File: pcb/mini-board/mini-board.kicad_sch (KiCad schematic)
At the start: 22 parts, among them J1 USB_B, J2 EXPBUS1, J4 Atmel-JTAG-10, SW1 RESET, SW2 NMI, SW3 SW_SPDT, U1 74AC14, U2 W65C02, U3 ATF1502AS-PLCC44, X1 14 MHz

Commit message: Expanding README.md
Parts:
- removed C5: 100nF, Capacitor_THT:C_Disc_D5.0mm_W2.5mm_P5.00mm, symbol Device:C
- removed J2: EXPBUS1, Connector_PinHeader_2.54mm:PinHeader_2x20_P2.54mm_Vertical, symbol Connector_Generic:Conn_02x20_Odd_Even
- removed R1, R4: 1k, Resistor_THT:R_Axial_DIN0207_L6.3mm_D2.5mm_P7.62mm_Horizontal, symbol Device:R
- removed SW1: RESET, Button_Switch_THT:SW_PUSH_6mm, symbol Switch:SW_Push
- removed U1: 74AC14, Package_DIP:DIP-14_W7.62mm_Socket, symbol 74xx:74HC14
- removed U3: ATF1502AS-PLCC44, Package_LCC:PLCC-44_THT-Socket, symbol atf1504as-plcc44:ATF1504AS-xJx44
- added C33, C34, C35, C36: 100nF, Capacitor_THT:C_Disc_D5.0mm_W2.5mm_P5.00mm, symbol Device:C
- added H1, H2, H3, H4: MountingHole, MountingHole:MountingHole_3.2mm_M3_DIN965_Pad_TopOnly, symbol Mechanical:MountingHole
- added J5: Conn_02x18_Odd_Even, Connector_PinHeader_2.54mm:PinHeader_2x18_P2.54mm_Vertical, symbol Connector_Generic:Conn_02x18_Odd_Even
- added R7, R9: 10k, Resistor_THT:R_Axial_DIN0207_L6.3mm_D2.5mm_P7.62mm_Horizontal, symbol Device:R
- added SW2: RESET, Button_Switch_THT:SW_PUSH_6mm, symbol Switch:SW_Push
- added U11: DS1813, Package_TO_SOT_THT:TO-92, symbol Connector:Conn_01x03_Pin
- added U23: ATF1502AS, Package_LCC:PLCC-44_THT-Socket, symbol atf1504_plcc44_breakout:ATF1504AS-xJx44
- C6: renamed from C7; value 10uF -> 220uF
- C7: renamed from C8; value 100uF -> 10uF; footprint Capacitor_THT:CP_Radial_D6.3mm_P2.50mm -> Capacitor_THT:CP_Radial_D5.0mm_P2.50mm
- R6: value 1k -> 10k
- X1: value 14 MHz -> CLK
- renumbered C6 to C9, R5 to R2, SW3 to SW1, SW2 to SW3
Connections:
- net A0: now also J5.3 (Pin_3)
- net A1: now also J5.5 (Pin_5)
- net A10: now also J5.23 (Pin_23), U23.6 (I/O)
- net A11: now also J5.25 (Pin_25), U23.8 (I/O)
- net A12: now also J5.27 (Pin_27), U23.9 (I/O)
- net A13: now also J5.29 (Pin_29), U23.11 (I/O/PD1)
- net A14: now also J5.31 (Pin_31), U23.12 (I/O)
- net A15: now also J5.33 (Pin_33), U23.14 (I/O)
- net A2: now also J5.7 (Pin_7)
- net A3: now also J5.9 (Pin_9)
- net A4: now also J5.11 (Pin_11)
- net A5: now also J5.13 (Pin_13)
- net A6: now also J5.15 (Pin_15), U23.21 (I/O)
- net A7: now also J5.17 (Pin_17), U23.2 (I/OE2/GCLK2)
- net A8: now also J5.19 (Pin_19), U23.4 (I/O)
- net A9: now also J5.21 (Pin_21), U23.5 (I/O)
- net CLK: now also X1.8 (OUT), J5.22 (Pin_22), U23.43 (I/GCLK1)
- net D0: now also J5.4 (Pin_4), U23.41 (I/O/GCLK3)
- net D1: now also J5.6 (Pin_6), U23.40 (I/O)
- net D2: now also J5.8 (Pin_8), U23.39 (I/O)
- net D3: now also J5.10 (Pin_10), U23.37 (I/O)
- net D4: now also J5.12 (Pin_12), U23.36 (I/O)
- net D5: now also J5.14 (Pin_14), U23.34 (I/O)
- net D6: now also J5.16 (Pin_16), U23.33 (I/O)
- net D7: now also J5.18 (Pin_18), U23.31 (I/O)
- net GND: now also C33.2, C34.2, C35.2, C36.2, J5.30 (Pin_30), J5.35 (Pin_35), J5.36 (Pin_36), SW2.1, U11.3 (Pin_3), U23.10 (GND), U23.22 (GND), U23.30 (GND), U23.42 (GND)
- net R/~{W}: now also J5.26 (Pin_26), U23.44 (I/OE1)
- net VCC: now also C33.1, C34.1, C35.1, C36.1, J5.1 (Pin_1), J5.2 (Pin_2), R7.2, R9.2, U11.2 (Pin_2), U23.15 (VCC), U23.23 (VCC), U23.3 (VCC), U23.35 (VCC)
- net ~{NMI}: now also J5.24 (Pin_24), R7.1; no longer R6.1
- net ~{RES}: now also J5.20 (Pin_20), SW2.2, U11.1 (Pin_1), U23.1 (I/GCLR)
- net at U2.2 (RDY): now also R9.1
- net JTAG_TCK renamed TCK
- net TCK: now also U23.32 (I/O/TCK)
- net JTAG_TDI renamed TDI
- net TDI: now also U23.7 (I/O/TDI)
- net JTAG_TDO renamed TDO
- net TDO: now also U23.38 (I/O/TDO)
- net JTAG_TMS renamed TMS
- net TMS: now also U23.13 (I/O/TMS)
- net ~{IRQC51_1} renamed ~{IRQ}
- net ~{IRQ}: now also R6.1, J5.28 (Pin_28)
- new net B0: U23.29 (I/O)
- new net B1: U23.28 (I/O)
- new net B2: U23.27 (I/O)
- new net B3: U23.26 (I/O)
- new net B4: U23.25 (I/O/PD2)
- new net B5: U23.24 (I/O)
- new net RxD1: J5.34 (Pin_34)
- new net TxD1: J5.32 (Pin_32)
- new net ~{RAM_CS}: U23.16 (I/O)
- new net ~{RAM_OE}: U23.17 (I/O)
- new net ~{ROM_CS}: U23.20 (I/O)
- new net ~{UART_CS}: U23.18 (I/O)
- new net ~{VIA_CS}: U23.19 (I/O)
- no-connect marks 19 -> 10
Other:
- removed sheet romram
- removed sheet uart
- added sheet peripherals (peripherals.kicad_sch)
- note removed: "Logical OR construction: If any of the ~{IRQ} request goes low (active), the CPU's ~{IRQ} will be triggered."
- note removed: "Schmidt inverters are used to clean the clock signal. Might require using 74AC21."
- note removed: "Unused gates are tied to GND"
- moved on the sheet: C3, C6, C7, J1, R2, SW1, X1

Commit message: Initial commit miniboard revision
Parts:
- U2: footprint Package_DIP:DIP-40_W15.24mm_Socket -> Package_DIP:DIP-40_W15.24mm
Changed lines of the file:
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@@
 			)
 		)
-		(property "Description" ""
+		(property "Description" "Power symbol creates a global label with name \"VCC\""
 			(at 104.14 27.94 0)
 			(effects
@@
 			)
 		)
-		(property "Footprint" "Package_DIP:DIP-40_W15.24mm_Socket"
+		(property "Footprint" "Package_DIP:DIP-40_W15.24mm"
 			(at 48.26 13.97 0)
 			(effects
@@
 			)
 		)
-		(property "Datasheet" " ~"
+		(property "Datasheet" "~"
 			(at 72.39 179.07 0)
 			(effects
@@
 			)
 		)
-		(property "Description" ""
+		(property "Description" "Power symbol creates a global label with name \"GND\" , ground"
 			(at 104.14 99.06 0)
 			(effects
@@
 			)
 		)
+		(property "Sim.Pins" "1=K 2=A"
+			(at 135.89 147.32 0)
+			(effects
+				(font
+					(size 1.27 1.27)
+				)
+				(hide yes)
+			)
+		)
 		(pin "1"
 		)
@@
 			)
 		)
-		(property "Description" ""
+		(property "Description" "Power symbol creates a global label with name \"GND\" , ground"
 			(at 264.16 104.14 0)
 			(effects
@@
 			)
 		)
-		(property "Description" ""
+		(property "Description" "Power symbol creates a global label with name \"VCC\""
 			(at 264.16 77.47 0)
 			(effects

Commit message: Fixing bugs in CPLD and removing minimalistic testrom
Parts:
- U2: footprint Package_DIP:DIP-40_W15.24mm -> Package_DIP:DIP-40_W15.24mm_Socket
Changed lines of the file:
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@@
 			)
 		)
-		(property "Footprint" "Package_DIP:DIP-40_W15.24mm"
+		(property "Footprint" "Package_DIP:DIP-40_W15.24mm_Socket"
 			(at 48.26 13.97 0)
 			(effects

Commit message: Pre-fourlayerboard commit
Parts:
- removed R6: 10k, Resistor_THT:R_Axial_DIN0207_L6.3mm_D2.5mm_P7.62mm_Horizontal, symbol Device:R
- added C4: 100nF, Capacitor_THT:C_Disc_D5.0mm_W2.5mm_P5.00mm, symbol Device:C
- added R10, R11, R12: 10k, Resistor_THT:R_Axial_DIN0207_L6.3mm_D2.5mm_P7.62mm_Horizontal, symbol Device:R
- added U1: 74AC11, Package_DIP:DIP-14_W7.62mm_Socket, symbol 74xx:74LS11
- J5: value Conn_02x18_Odd_Even -> SYSTEM BUS; footprint Connector_PinHeader_2.54mm:PinHeader_2x18_P2.54mm_Vertical -> Connector_PinHeader_2.54mm:PinHeader_2x20_P2.54mm_Vertical; symbol Connector_Generic:Conn_02x18_Odd_Even -> Connector_Generic:Conn_02x20_Odd_Even
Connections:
- net GND: now also J5.39 (Pin_39), J5.40 (Pin_40), C4.2, U1.1, U1.13, U1.2, U1.7 (GND); no longer J5.30 (Pin_30), J5.35 (Pin_35), J5.36 (Pin_36)
- net RxD1: now also J5.38 (Pin_38); no longer J5.34 (Pin_34)
- net TxD1: now also J5.36 (Pin_36); no longer J5.32 (Pin_32)
- net VCC: now also C4.1, R10.1, R11.1, R12.1, U1.14 (VCC)
- net ~{IRQ}: now also U1.8
- new net: U1.6, U1.9
- new net ~{IRQ0}: J5.30 (Pin_30), R10.2, U1.3
- new net ~{IRQ1}: J5.32 (Pin_32), R11.2, U1.4
- new net ~{IRQ22}: J5.35 (Pin_35), U1.10
- new net ~{IRQ2}: J5.34 (Pin_34), R12.2, U1.5
- new net ~{IRQ51}: J5.37 (Pin_37), U1.11
- no-connect marks 10 -> 11

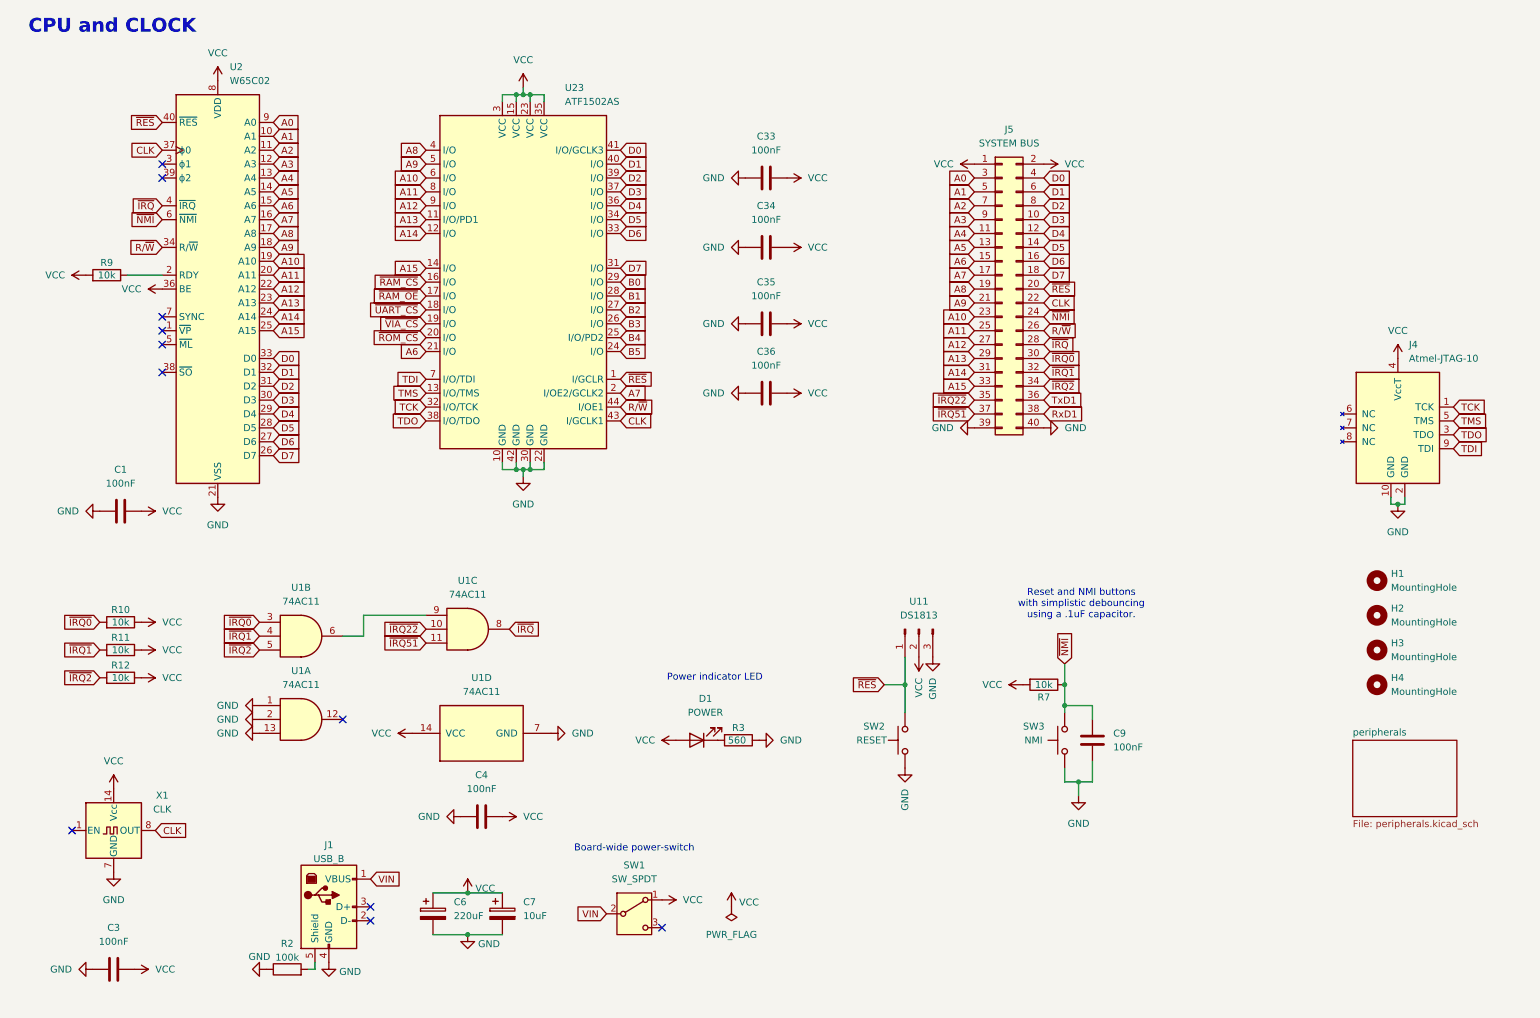
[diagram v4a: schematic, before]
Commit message: Adding documentation to schematics
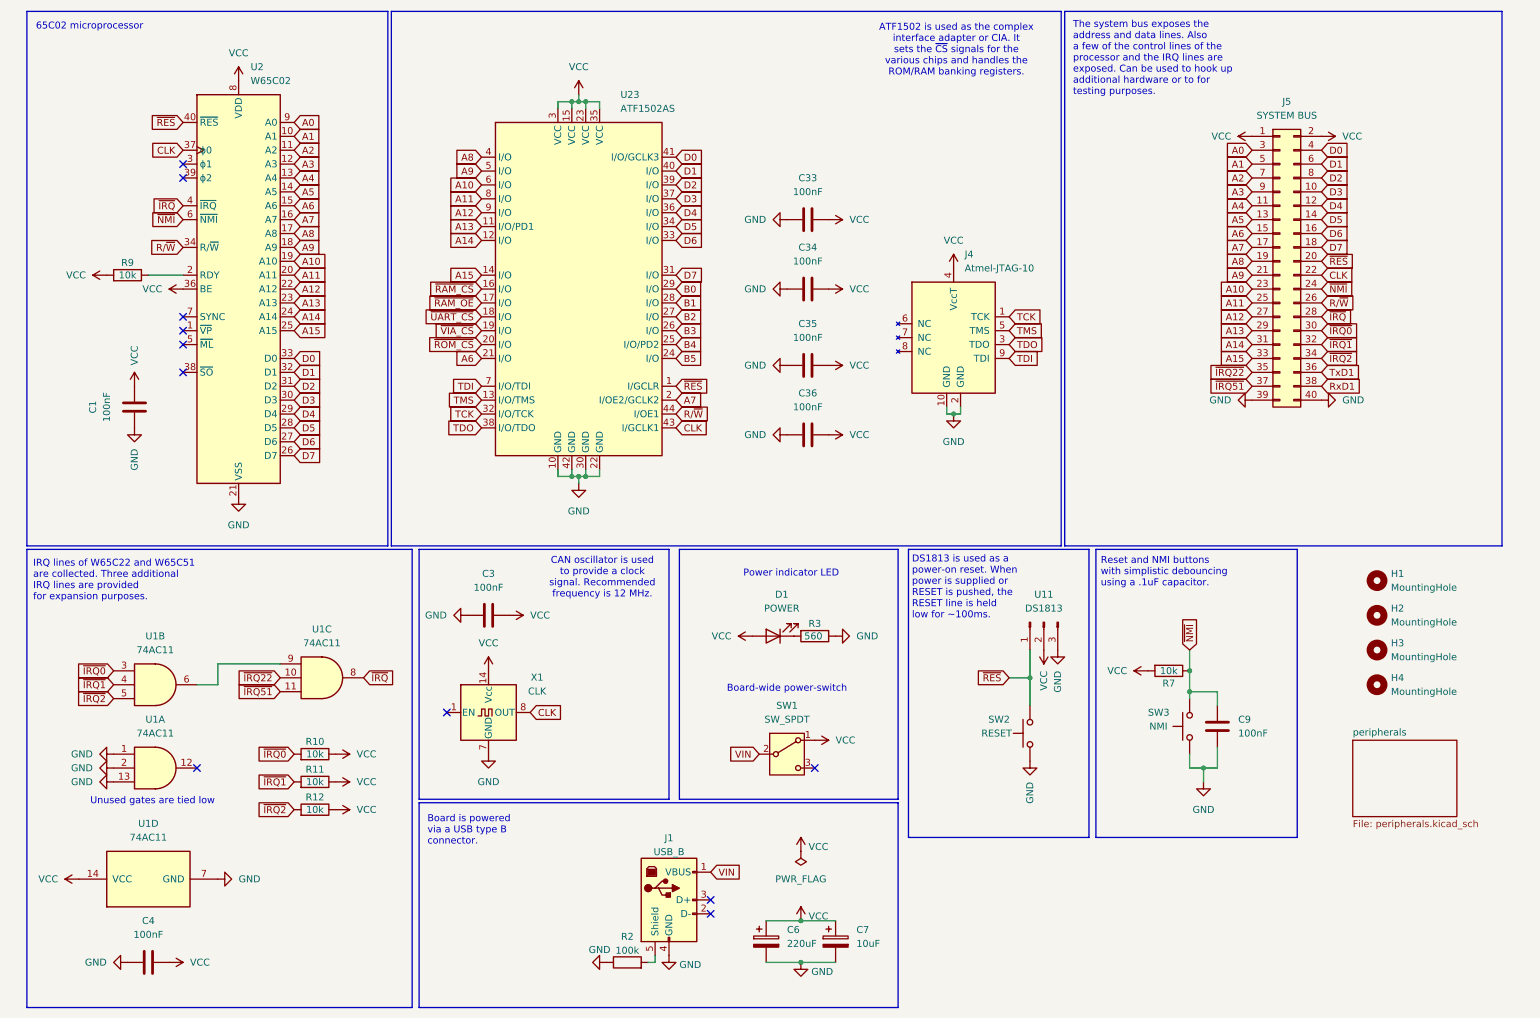
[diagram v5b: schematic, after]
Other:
- note added: "65C02 microprocessor"
- note added: "ATF1502 is used as the complex interface adapter or CIA. It sets the ~{CS} signals for the various chips and handles the ROM/RAM banking registers."
- note added: "Board is powered via a USB type B connector."
- note added: "CAN oscillator is used to provide a clock signal. Recommended frequency is 12 MHz."
- note added: "DS1813 is used as a power-on reset. When power is supplied or RESET is pushed, the RESET line is held low for ~100ms."
- note added: "IRQ lines of W65C22 and W65C51 are collected. Three additional IRQ lines are provided for expansion purposes."
- note added: "The system bus exposes the address and data lines. Also a few of the control lines of the processor and the IRQ lines are exposed. Can be used to hook up additional hardware or to for testing purposes."
- note added: "Unused gates are tied low"
- note removed: "CPU and CLOCK"
- moved on the sheet: C1, C3, C33, C34, C35, C36, C4, C6, C7, C9, D1, J1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

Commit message: Exporting pages
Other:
- title: ByteCradle 6502 - CPU & CLOCK -> ByteCradle 6502 MINI BOARD
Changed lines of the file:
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@@
 	(paper "A4")
 	(title_block
-		(title "ByteCradle 6502 - CPU & CLOCK")
-		(date "2025-01-25")
+		(title "ByteCradle 6502 MINI BOARD")
+		(date "2025-05-03")
 		(rev "rev1")
 	)
